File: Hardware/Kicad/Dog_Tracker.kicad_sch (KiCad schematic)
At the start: 19 parts, among them IC1 M4 Feather, U1 ADP160AUJZ-1.8-R7, U2 SX1280IMLTRT, U3 Origin_GPS1510, U4 NFA18SL407V1A45L, U5 SN74AUP1T97, U6 LSM6DSO32

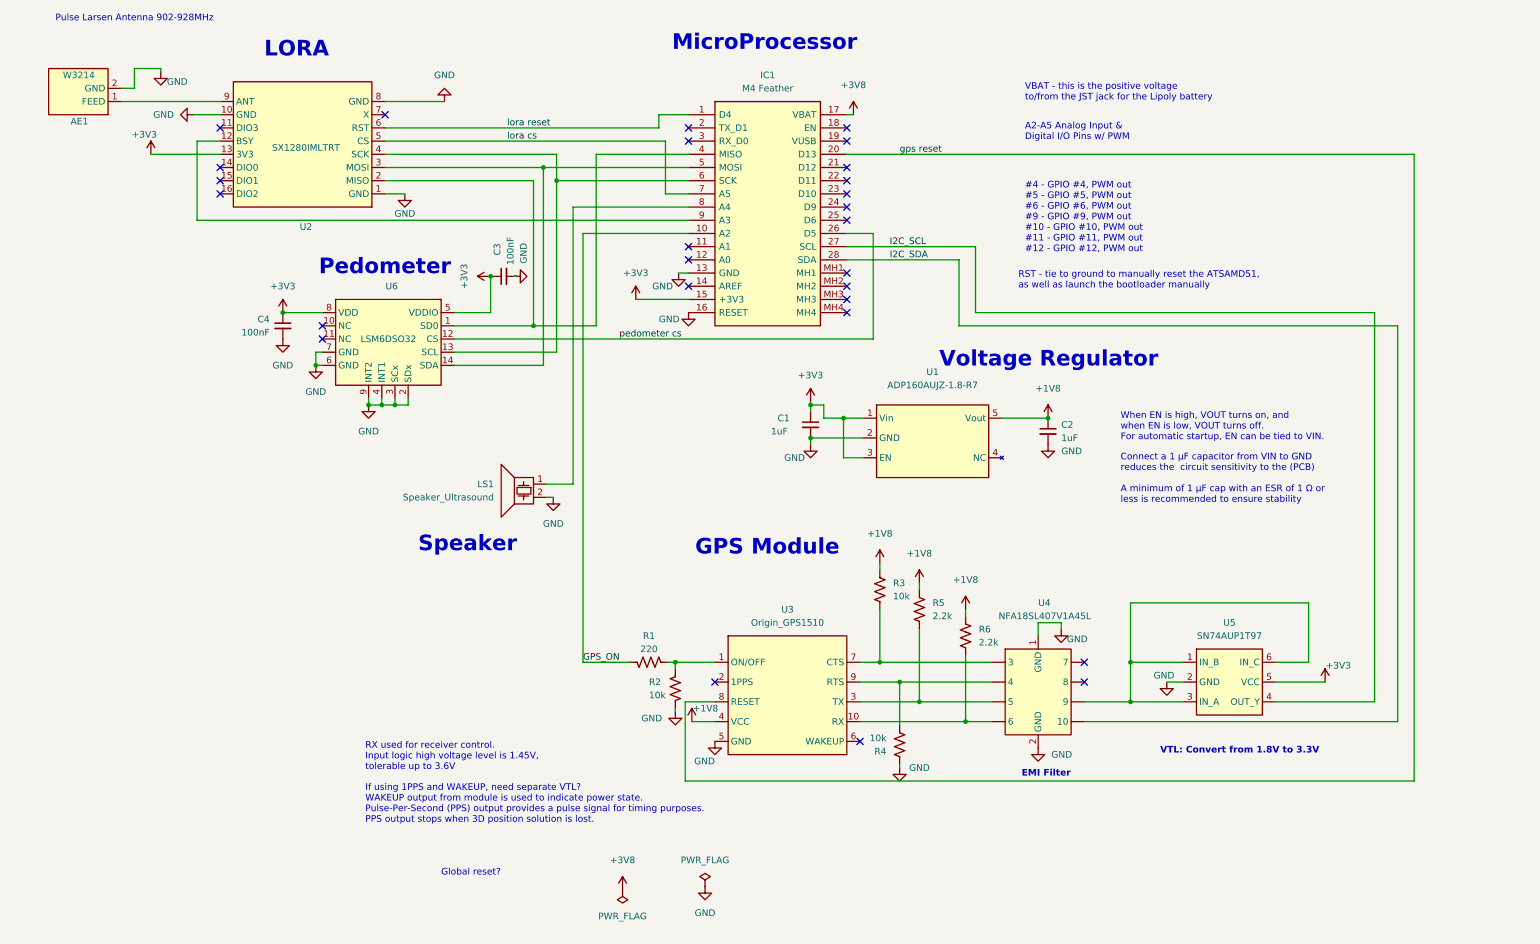
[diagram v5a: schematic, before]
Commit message: removed footprints and added the origin gps only. updated schematic per steves feedback
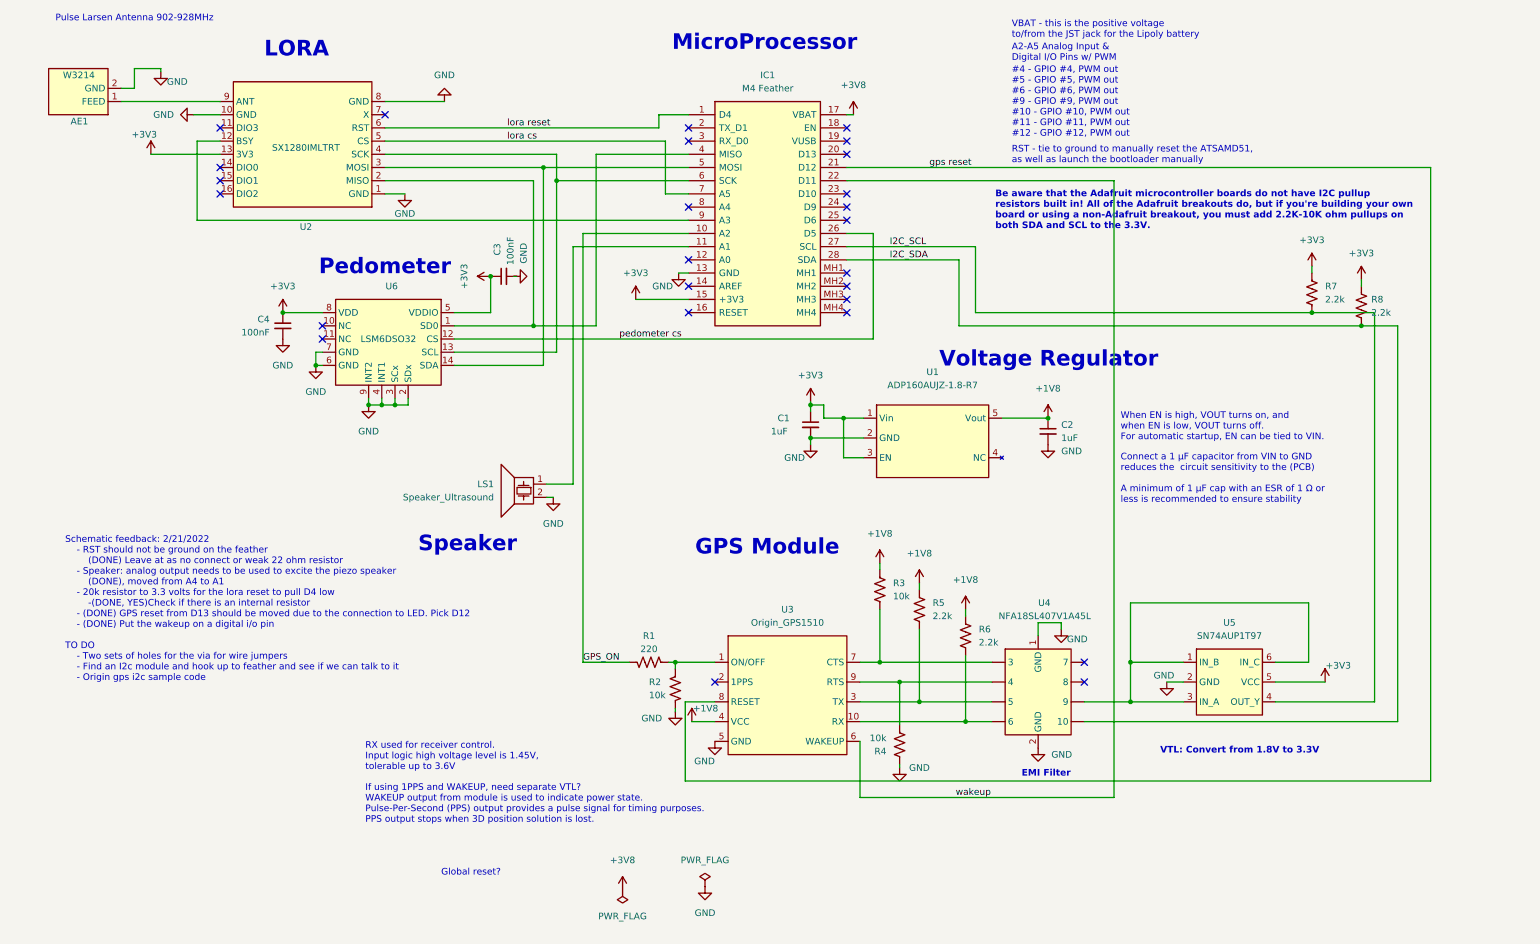
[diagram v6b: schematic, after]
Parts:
- added R7, R8: 2.2k, Resistor_SMD:R_0402_1005Metric, symbol Device:R_US
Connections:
- net +3V3: now also R7.2, R8.2
- net GND: no longer IC1.16 (RESET)
- net I2C_SCL: now also R7.1
- net I2C_SDA: now also R8.1
- net gps reset: now also IC1.21 (D12); no longer IC1.20 (D13)
- net at LS1.1: now also IC1.11 (A1); no longer IC1.8 (A4)
- net wakeup: now reaches U3.6 (WAKEUP)
- net wakeup: now also IC1.22 (D11)
- no-connect marks 27 -> 26
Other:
- note added: "Be aware that the Adafruit microcontroller boards do not have I2C pullup resistors built in! All of the Adafruit breakouts do, but if you're building your own board or using a non-Adafruit breakout, you must add 2.2K-10K ohm pullups on both SDA and SCL to the 3.3V."
- note added: "Schematic feedback: 2/21/2022 - RST should not be ground on the feather (DONE) Leave at as no connect or weak 22 ohm resistor - Speaker: analog output needs to be used to excite the piezo speaker (DONE), moved from A4 to A1 - 20k resistor to 3.3 volts for the lora reset to pull D4 low -(DONE, YES)Check if there is an internal resistor - (DONE) GPS reset from D13 should be moved due to the connect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"

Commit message: added footprints
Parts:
- IC1: footprint 3857 -> Dog_Tracker:Feather_M4
- U1: footprint Dog_Tracker:ADP160AUJZ-1.8-R7 -> Dog_Tracker:SOT95P280X100
- U3: footprint Dog_Tracker:OriginGPS_LTD-ORG1510-MK04-0 -> Dog_Tracker:ORG1510
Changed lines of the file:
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@@
     (property "Reference" "U3" (id 0) (at 159.385 127.635 0))
     (property "Value" "Origin_GPS1510" (id 1) (at 159.385 130.175 0))
-    (property "Footprint" "Dog_Tracker:OriginGPS_LTD-ORG1510-MK04-0" (id 2) (at 159.385 128.905 0)
+    (property "Footprint" "Dog_Tracker:ORG1510" (id 2) (at 159.385 128.905 0)
       (effects (font (size 1.27 1.27)) hide)
     )
@@
     (property "Reference" "IC1" (id 0) (at 155.575 24.765 0))
     (property "Value" "M4 Feather" (id 1) (at 155.575 27.305 0))
-    (property "Footprint" "3857" (id 2) (at 167.005 29.845 0)
+    (property "Footprint" "Dog_Tracker:Feather_M4" (id 2) (at 167.005 29.845 0)
       (effects (font (size 1.27 1.27)) (justify left) hide)
     )
@@
     (property "Reference" "U1" (id 0) (at 187.325 81.915 0))
     (property "Value" "ADP160AUJZ-1.8-R7" (id 1) (at 187.325 84.455 0))
-    (property "Footprint" "Dog_Tracker:ADP160AUJZ-1.8-R7" (id 2) (at 186.69 84.455 0)
+    (property "Footprint" "Dog_Tracker:SOT95P280X100" (id 2) (at 186.69 84.455 0)
       (effects (font (size 1.27 1.27)) hide)
     )
@@
     )
     (path "/a645b044-60df-4845-a737-a91e49f25a7b"
-      (reference "IC1") (unit 1) (value "M4 Feather") (footprint "3857")
+      (reference "IC1") (unit 1) (value "M4 Feather") (footprint "Dog_Tracker:Feather_M4")
     )
     (path "/42b2a1f3-180d-403b-b90d-f6dcca840918"
@@
     )
     (path "/c50a4250-2225-4797-b4a1-1bc3d1138c0f"
-      (reference "U1") (unit 1) (value "ADP160AUJZ-1.8-R7") (footprint "Dog_Tracker:ADP160AUJZ-1.8-R7")
+      (reference "U1") (unit 1) (value "ADP160AUJZ-1.8-R7") (footprint "Dog_Tracker:SOT95P280X100")
     )
     (path "/82cef259-9dd0-43ea-9ad2-d4e5547a5601"
@@
     )
     (path "/49389a66-8741-452b-8284-834f65c51e1b"
-      (reference "U3") (unit 1) (value "Origin_GPS1510") (footprint "Dog_Tracker:OriginGPS_LTD-ORG1510-MK04-0")
+      (reference "U3") (unit 1) (value "Origin_GPS1510") (footprint "Dog_Tracker:ORG1510")
     )
     (path "/f4f8401f-00e2-4058-8b4d-acf3075d7f77"

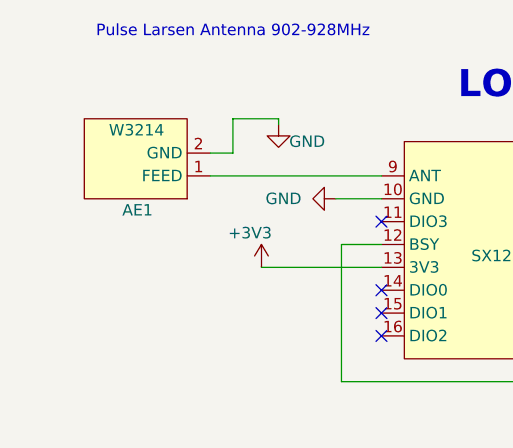
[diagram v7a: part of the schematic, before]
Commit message: 'update 3214 to 3211'
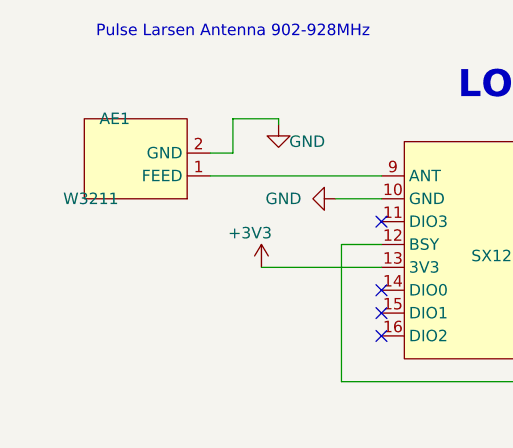
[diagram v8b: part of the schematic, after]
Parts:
- AE1: value W3214 -> W3211
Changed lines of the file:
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@@
   (symbol (lib_id "Dog_Tracker:W3214") (at 23.495 28.575 180) (unit 1)
     (in_bom yes) (on_board yes)
-    (property "Reference" "AE1" (id 0) (at 24.765 33.655 0)
-      (effects (font (size 1.27 1.27)) (justify left))
-    )
-    (property "Value" "W3214" (id 1) (at 26.035 24.765 0)
+    (property "Reference" "AE1" (id 0) (at 22.225 23.495 0)
+      (effects (font (size 1.27 1.27)) (justify left))
+    )
+    (property "Value" "W3211" (id 1) (at 20.955 32.385 0)
       (effects (font (size 1.27 1.27)) (justify left))
     )
@@
     )
     (path "/b60171e3-1072-4d20-a3d0-5c124c2b7fc1"
-      (reference "AE1") (unit 1) (value "W3214") (footprint "")
+      (reference "AE1") (unit 1) (value "W3211") (footprint "")
     )
     (path "/a82c7da7-6077-4900-b925-87315eda8158"
